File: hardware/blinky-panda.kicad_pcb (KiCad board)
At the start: 2 copper layers, 69.5 x 56.4 mm, 36 parts, among them J1 AVR-ISP-6, SW1 SW_SPDT, SW2 SW_Push, U1 ATtiny84A-PU

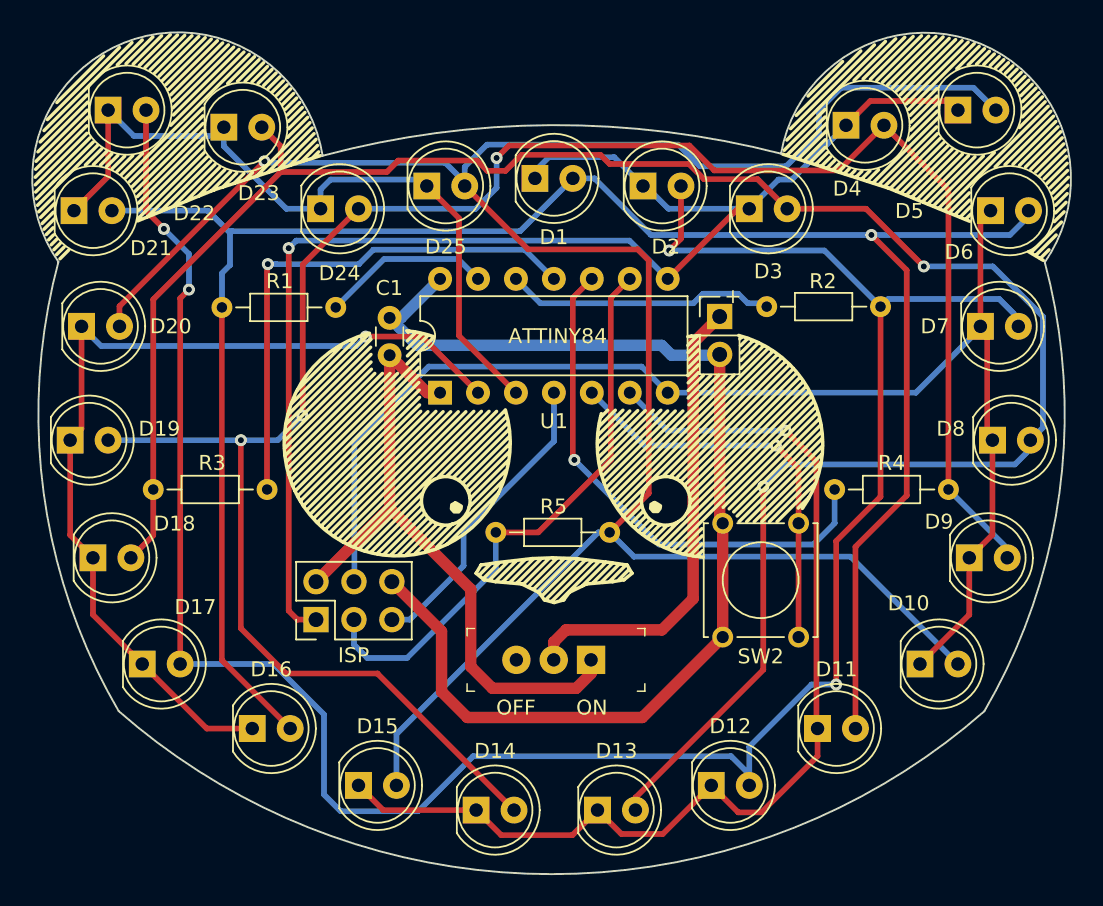
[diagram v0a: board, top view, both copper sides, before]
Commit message: rework pin assignments to fix isp
I thought maybe it'd be a bad idea to have SCK connected to MOSI
through a 220 ohm resistor.

in this arrangement, power won't flow from one programming pin
to another (they'll all hit reverse diodes)
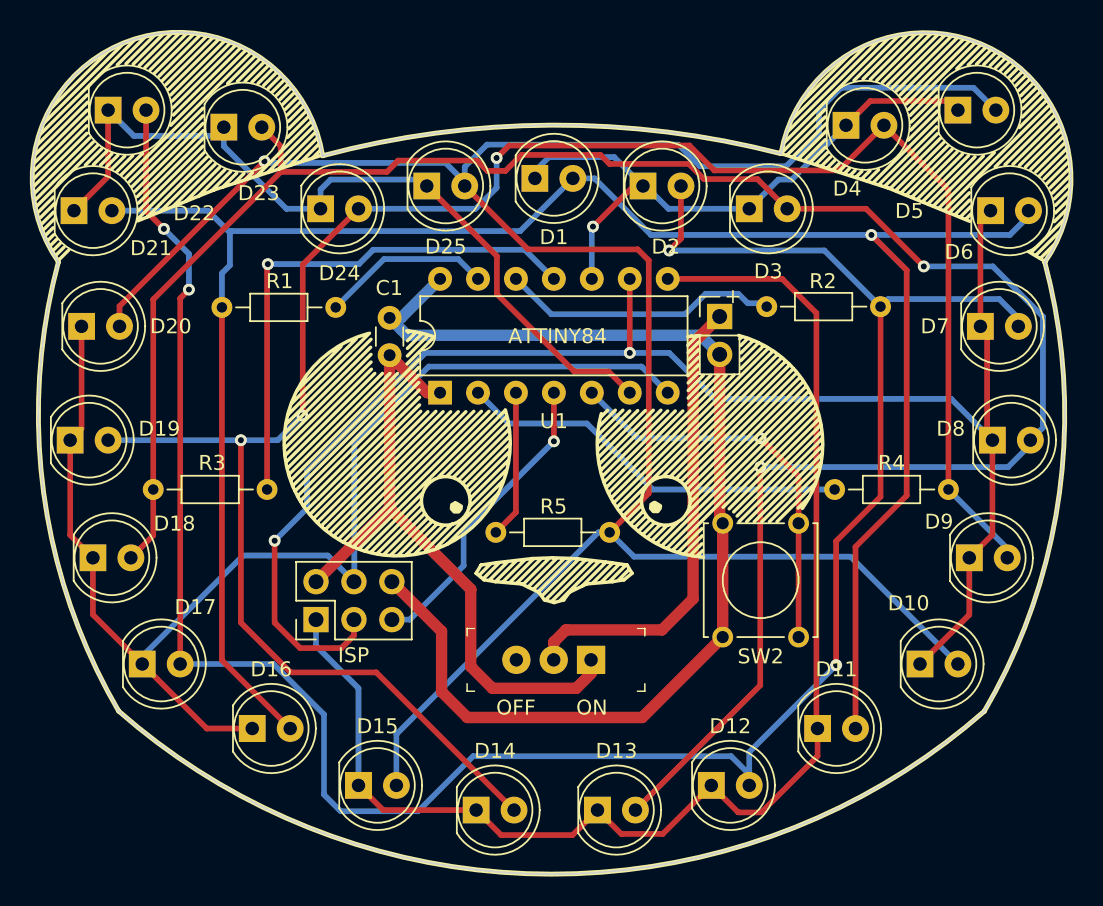
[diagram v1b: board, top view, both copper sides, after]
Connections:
- D1 pad 1: /col4 -> /col0
- D10 pad 1: /col3 -> /col1
- D16 pad 1: /col1 -> /col3
- D17 pad 1: /col1 -> /col3
- D18 pad 1: /col1 -> /col3
- D19 pad 1: /col1 -> /col3
- D2 pad 1: /col4 -> /col0
- D20 pad 1: /col1 -> /col3
- D21 pad 1: /col0 -> /col4
- D22 pad 1: /col0 -> /col4
- D23 pad 1: /col0 -> /col4
- D24 pad 1: /col0 -> /col4
- D25 pad 1: /col0 -> /col4
- D3 pad 1: /col4 -> /col0
- D4 pad 1: /col4 -> /col0
- D5 pad 1: /col4 -> /col0
- D6 pad 1: /col3 -> /col1
- D7 pad 1: /col3 -> /col1
- D8 pad 1: /col3 -> /col1
- D9 pad 1: /col3 -> /col1
- J1 pad 1: /col4 -> /col2
- J1 pad 3: /row4 -> /col1
- U1 pad 10: /row3 -> /col0
- U1 pad 2: /col1 -> /row3
- U1 pad 3: /col0 -> /row4
- U1 pad 6: /col2 -> /col4
- U1 pad 8: /col4 -> /col2
- U1 pad 9: /row4 -> /col1
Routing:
- net /col1: track 63.0 -> 108.0 mm, vias 1 -> 2
- net /col4: track 94.3 -> 55.5 mm, vias 1 -> 0
- net /row4: track 38.8 -> 9.91 mm
- net /col2: track 71.3 -> 90.0 mm, vias 1 -> 0
- net /col0: track 51.0 -> 41.9 mm, vias 0 -> 1
- net /row3: track 35.3 -> 26.6 mm, vias 1 -> 0
- net /col3: track 89.0 -> 85.5 mm
- net Net-(D12-Pad2): track 154.1 -> 153.2 mm
- net Net-(D13-Pad2): track 143.4 -> 144.1 mm
- net /row1: track 18.1 -> 18.7 mm
- net /rst: vias 0 -> 1

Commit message: tagline
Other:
- board text added: "github.com/jstanley0/blinky-panda"

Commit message: test
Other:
- board text added: "JLCJLCJLCJLC"
- board text removed: "ATTINY84"
